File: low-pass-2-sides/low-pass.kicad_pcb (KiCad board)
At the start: 2 copper layers, 29.1 x 16 mm, 11 parts, among them J1 Conn_Coaxial, J2 Conn_Coaxial

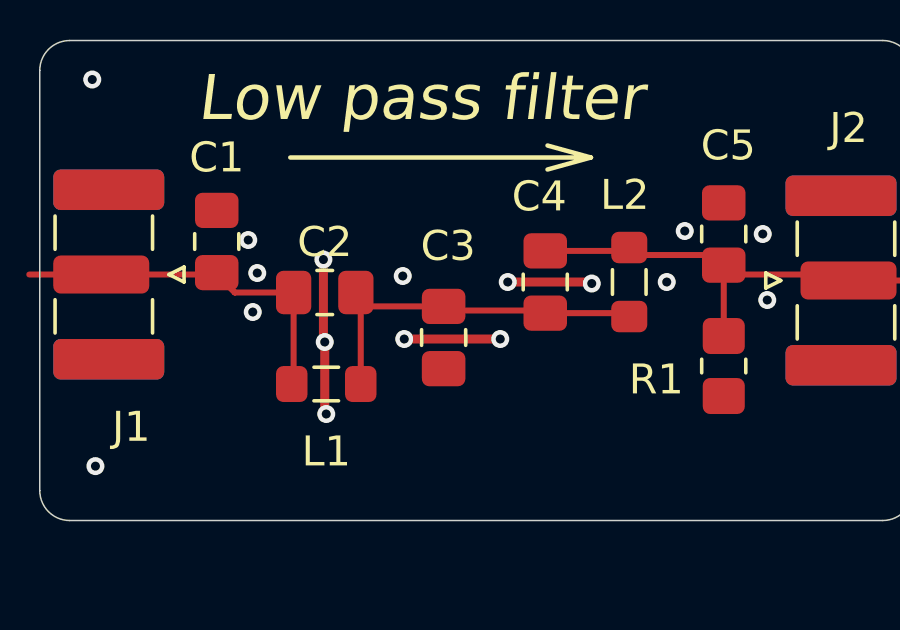
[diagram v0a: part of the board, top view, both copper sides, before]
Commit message: Improved (I think) the two layer layout
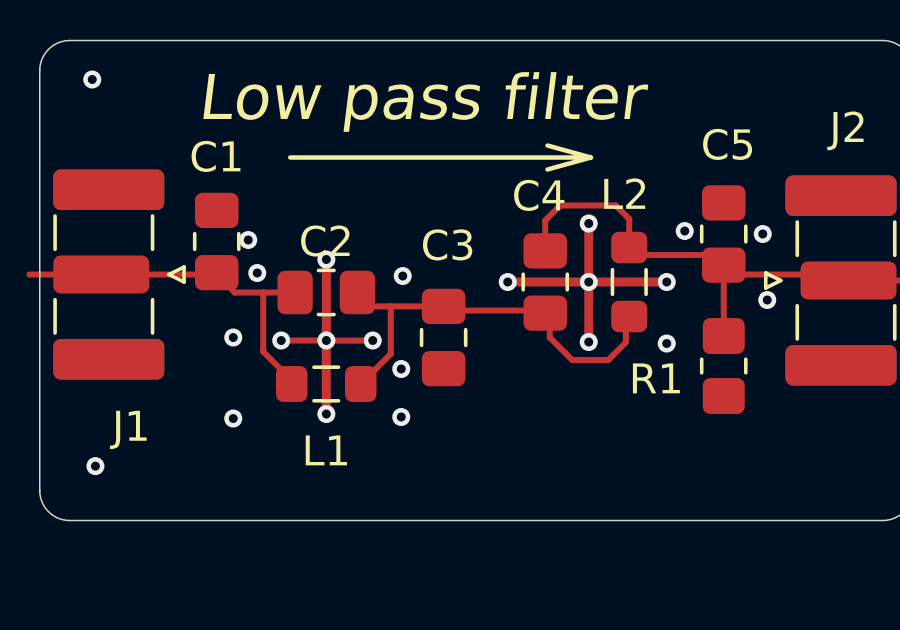
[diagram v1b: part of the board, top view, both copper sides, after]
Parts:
- moved C2 0.05 mm to (126.2, 75.4)
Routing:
- net GND: track 11.2 -> 17.9 mm, vias 17 -> 23
- net Net-(J2-In): track 14.6 -> 17.0 mm
- net Net-(C2-Pad2): track 12.4 -> 14.8 mm
